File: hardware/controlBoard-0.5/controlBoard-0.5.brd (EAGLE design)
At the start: 50.8 x 22.9 mm, 15 parts, among them J1 AYZ0202

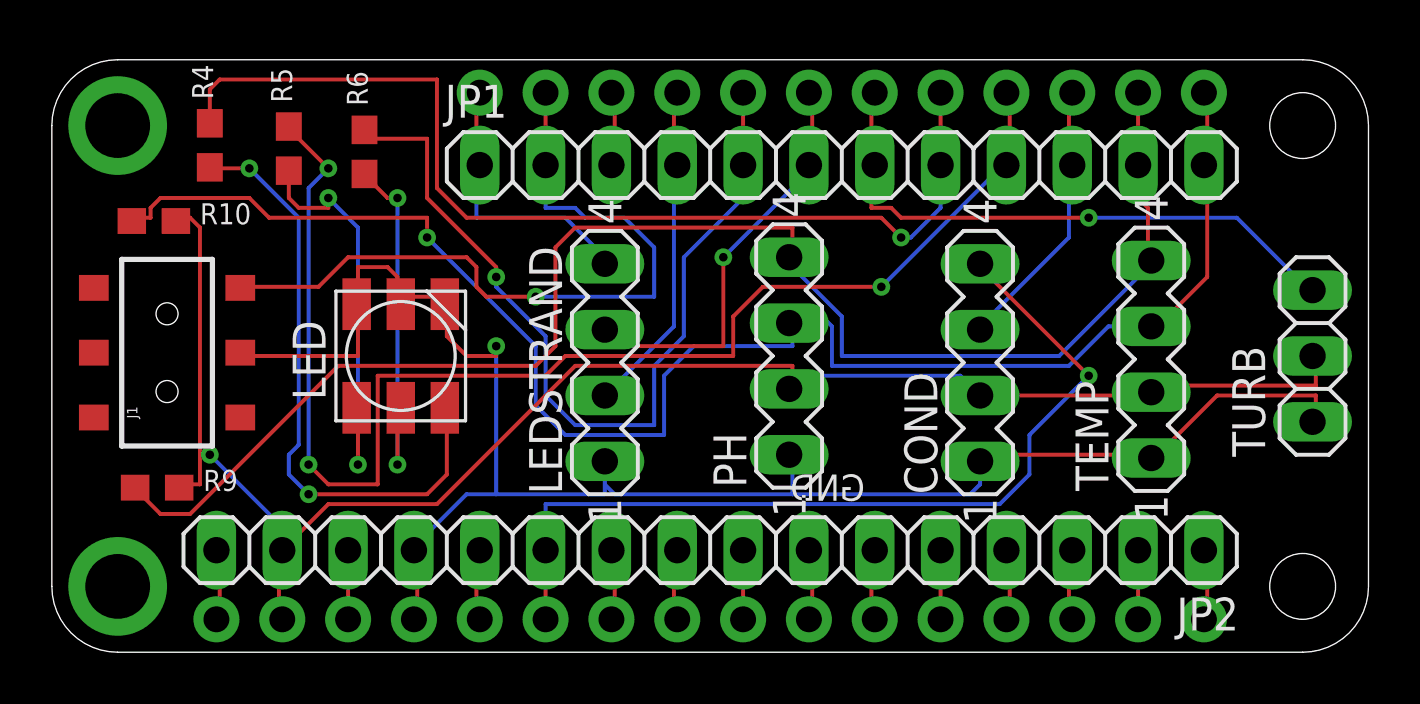
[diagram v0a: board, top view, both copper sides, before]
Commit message: control board update
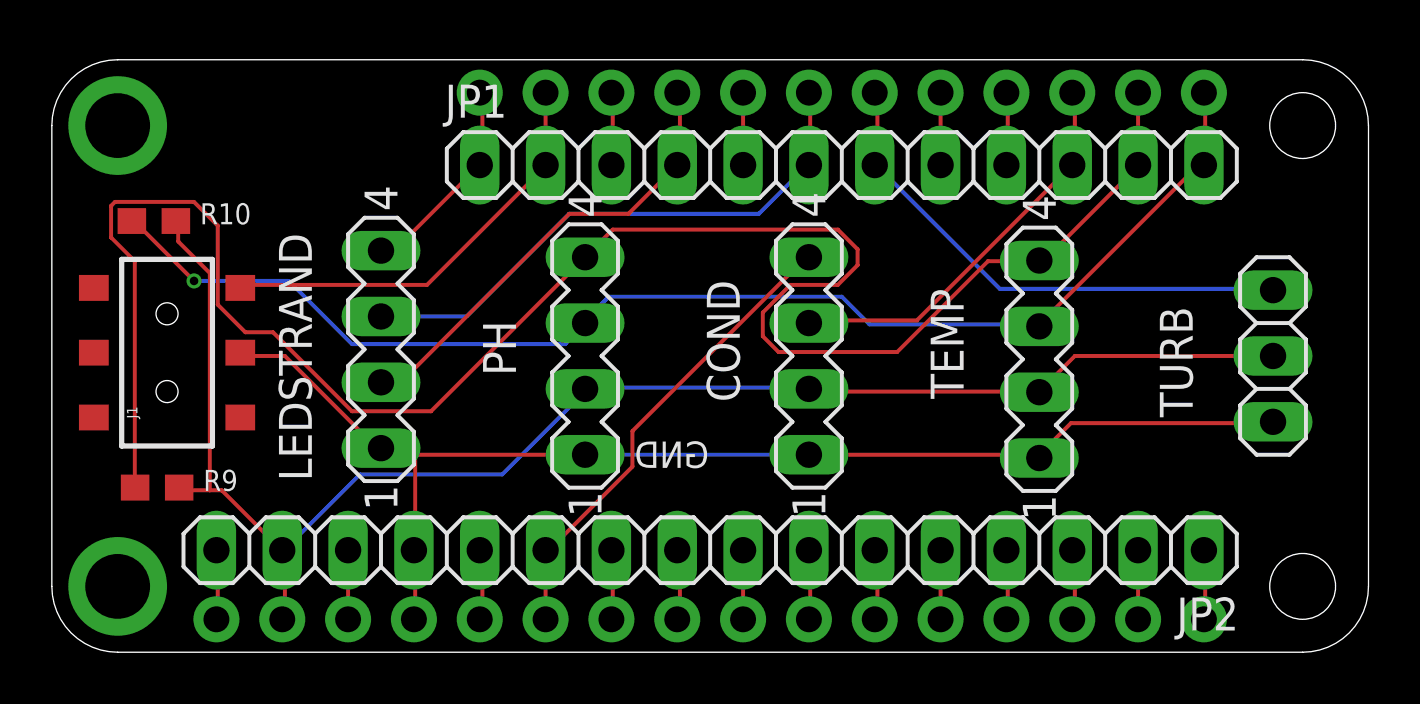
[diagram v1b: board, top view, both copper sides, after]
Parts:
- removed LED: (no value), adafruit:RGBLED5050
- removed R4, R5, R6: 10K, microbuilder:0603-NO
- moved LEDSTRAND 8.65 mm to (12.7, 11.7)
- moved PH 7.87 mm to (20.6, 11.4)
- moved COND 6.61 mm to (29.2, 11.4)
- moved TEMP 4.32 mm to (38.1, 11.3)
- moved TURB 1.52 mm to (47.1, 11.4)
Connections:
- removed net N$1: LED.2, R6.1
- removed net N$22: LED.3, R4.1
- removed net N$23: LED.1, R5.1
- net D12: no longer R6.2
- net D6: no longer R5.2
- net D9: no longer R4.2
- net GND: no longer LED.4, LED.5, LED.6
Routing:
- net D6: track 52.5 -> 2.82 mm, vias 3 -> 0
- net D9: track 39.6 -> 2.79 mm, vias 1 -> 0
- net D12: track 33.4 -> 2.79 mm, vias 1 -> 0
- net N$22: track 23.6 -> 0.00 mm, vias 2 -> 0
- net GND: track 67.2 -> 50.0 mm, vias 1 -> 0
- net SCL: track 58.8 -> 75.0 mm
- net N$23: track 16.1 -> 0.00 mm, vias 2 -> 0
- net A1: track 34.4 -> 18.4 mm, vias 1 -> 0
- net N$1: track 14.2 -> 0.00 mm, vias 2 -> 0
- net SDA: track 62.5 -> 50.2 mm
- net EN: track 28.7 -> 16.6 mm, vias 1 -> 0
- net VCC: track 65.9 -> 60.2 mm, vias 1 -> 0
- net D11: track 16.2 -> 21.7 mm, vias 1 -> 0
- net D5: track 10.7 -> 15.6 mm
- net D13: track 12.9 -> 17.8 mm
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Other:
- board text added: "6.26.18"
- board text added: "controlboard-0.5"
- board text removed: "fishnet-0.5 2.13.18"

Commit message: hardware update
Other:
- board text added: "controlboard v0.5"
- board text removed: "controlboard-0.5"
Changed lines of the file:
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@@
 <dimension x1="2.54" y1="2.667" x2="2.413" y2="20.32" x3="-2.159" y3="11.4935" textsize="3.5" layer="47" dtype="vertical"/>
 <dimension x1="3.81" y1="20.193" x2="1.27" y2="20.447" x3="2.54" y3="23.622" textsize="3.5" layer="47" dtype="horizontal"/>
-<text x="7.239" y="22.098" size="1.778" layer="26" rot="MR270">controlboard-0.5</text>
+<text x="9.017" y="21.844" size="1.778" layer="26" rot="MR270">controlboard
+v0.5</text>
 <text x="14.478" y="8.128" size="1.016" layer="26" rot="MR180">GND</text>
 <text x="47.752" y="11.303" size="1.016" layer="26" rot="MR180">VCC</text>
@@
 <text x="48.133" y="15.748" size="1.016" layer="26" rot="MR180">D10</text>
 <text x="50.419" y="7.239" size="1.016" layer="26" rot="MR0">GND</text>
-<text x="42.926" y="6.858" size="1.016" layer="26" rot="MR0">GND</text>
+<text x="43.18" y="6.858" size="1.016" layer="26" rot="MR0">GND</text>
 <text x="34.163" y="7.112" size="1.016" layer="26" rot="MR0">GND</text>
-<text x="22.479" y="8.128" size="1.016" layer="25" rot="MR180">GND</text>
+<text x="22.479" y="8.128" size="1.016" layer="26" rot="MR180">GND</text>
 <text x="39.878" y="10.541" size="1.016" layer="26" rot="MR180">VCC</text>
 <text x="31.115" y="10.668" size="1.016" layer="26" rot="MR180">VCC</text>
@@
 </board>
 </drawing>
+<compatibility>
+<note version="6.3" minversion="6.2.2" severity="warning">
+Since Version 6.2.2 text objects can contain more than one line,
+which will not be processed correctly with this version.
+</note>
+</compatibility>
 </eagle>
